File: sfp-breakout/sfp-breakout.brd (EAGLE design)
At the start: 65 x 65 mm, 29 parts, among them IC1 TLV1117-25, J1 694108106102, X1 PINHD-1X4LOCK, X2 PINHD-1X4LOCK

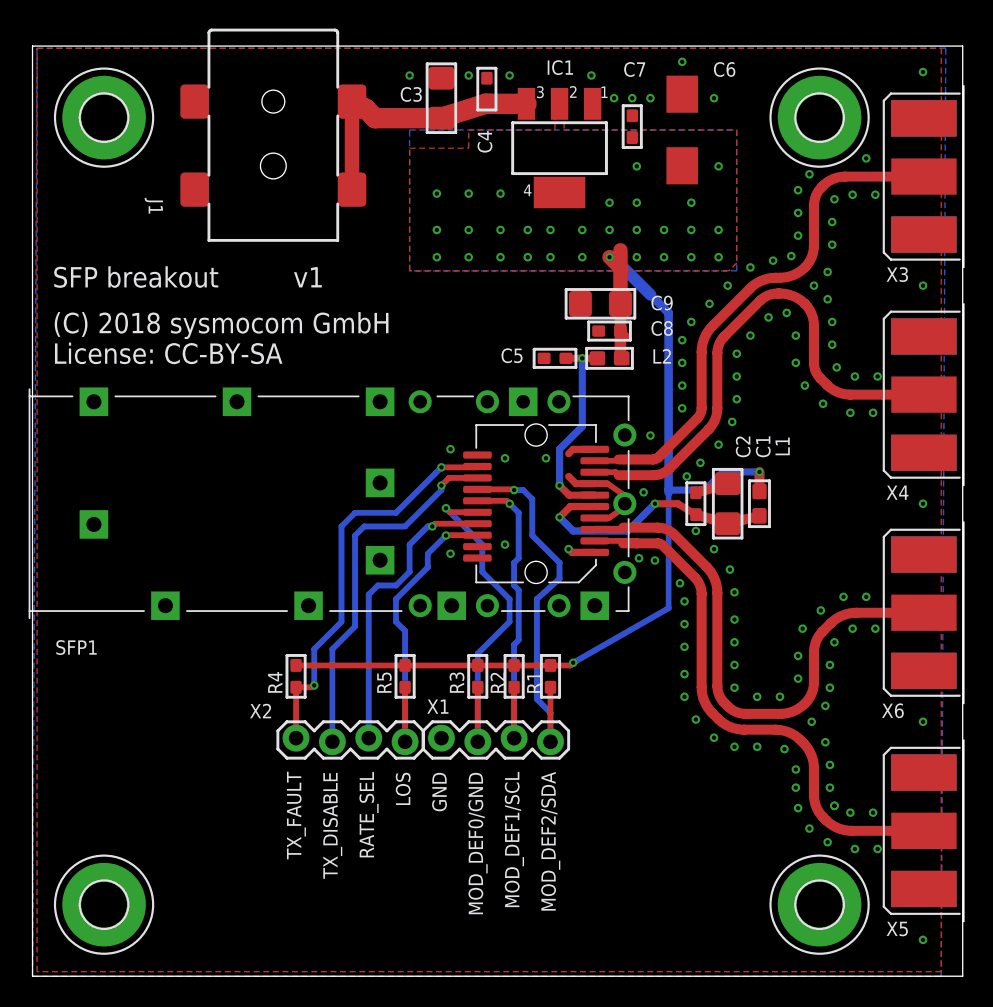
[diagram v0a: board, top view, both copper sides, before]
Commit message: spf: revise both SFP designs (OSM#3313/OSM#3314)
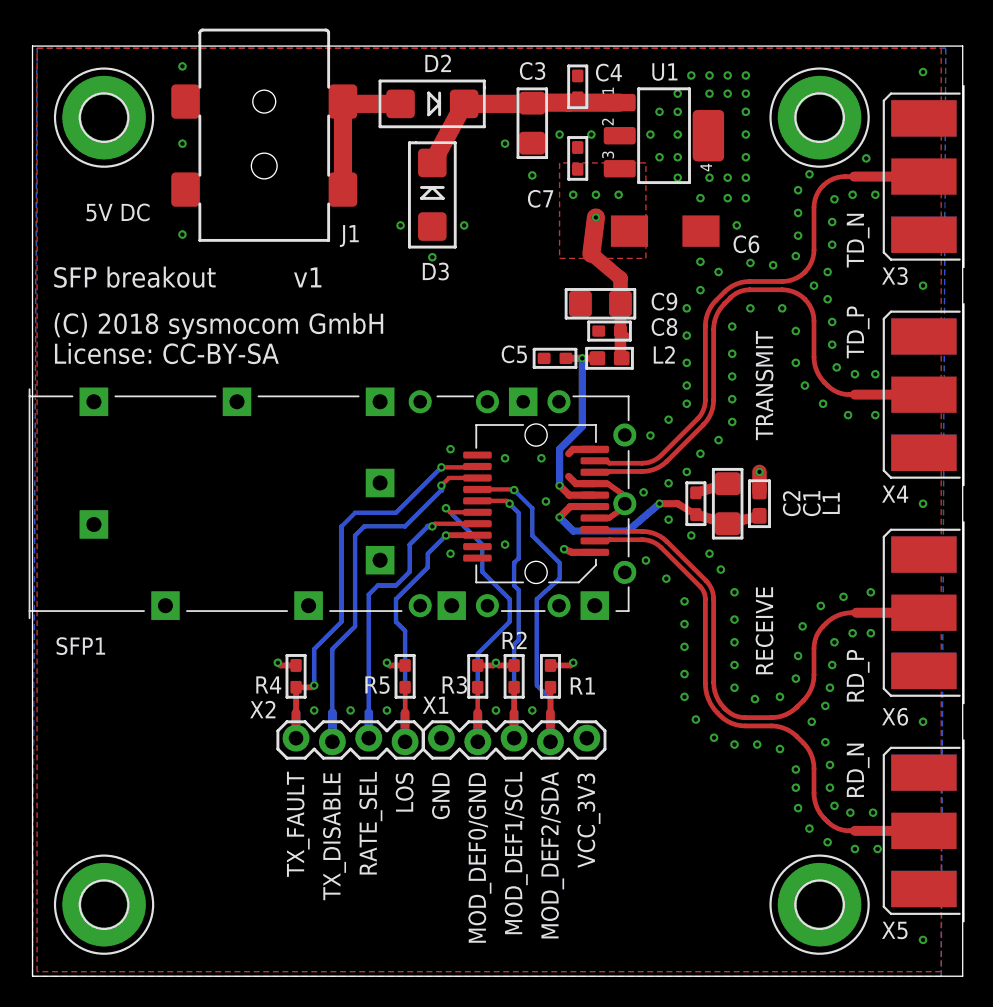
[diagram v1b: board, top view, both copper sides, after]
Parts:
- removed IC1: TLV1117-25, sfp-experimenter:SOT223
- added D2: SS16T3G, sfp-breakout:SMADIODE
- added D3: 824500500, sfp-breakout:SMADIODE
- added U1: LDO-MCP1825S, sfp-breakout:SOT223
- C1, C3, C9: device sfp-experimenter:CPOL1206 -> sfp-breakout:CPOL1206
- C2, C4, C5, C7, C8, R1, R2, R3, R4, R5: device sfp-experimenter:_0603 -> sfp-breakout:_0603
- H1, H2, H3, H4: device sfp-experimenter:3,2-PAD -> sfp-breakout:3,2-PAD
- J1: device sfp-experimenter:694108106102 -> sfp-breakout:694108106102
- L1, L2: device sfp-experimenter:0603 -> sfp-breakout:0603
- SFP1: device sfp-experimenter:SFP_COMBINED -> sfp-breakout:SFP_COMBINED
- X1: value PINHD-1X4LOCK -> PINHD-1X5LOCK; device sfp-experimenter:1X04_LOCK -> sfp-breakout:1X05_LOCK
- X2: device sfp-experimenter:1X04_LOCK -> sfp-breakout:1X04_LOCK
- X3, X4, X5, X6: device sfp-experimenter:SMA-F-S-EDGE -> sfp-breakout:SMA-F-S-EDGE
- moved C6 7.16 mm to (44.2, 52.1), turned to 0 degrees
- moved C3 6.59 mm to (34.9, 59.6), turned to 90 degrees
- moved C4 6.35 mm to (38.1, 62.2)
- moved C7 4.41 mm to (38.1, 57.1)
- moved J1 0.64 mm to (16.2, 66.1)
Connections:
- new net N$1: D2.A, J1.1, J1.1-1
- net +VIN: now also D2.C, D3.C, U1.1; no longer IC1.3, J1.1, J1.1-1
- net GND: now also D3.A, U1.2, U1.4; no longer IC1.1
- net VCC_3V3: now also U1.3; no longer IC1.2, IC1.4
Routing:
- net VCC_3V3: track 71.1 -> 19.9 mm, vias 32 -> 9
- net N$1: track 0.00 -> 10.5 mm
- net +VIN: track 19.6 -> 16.3 mm
- net TX_FAULT: track 28.0 -> 29.8 mm
- net RD_N: track 38.3 -> 37.0 mm
- net TD_N: track 36.0 -> 37.1 mm
- net TD_P: track 35.9 -> 36.8 mm
- net GND: track 14.2 -> 14.5 mm, vias 116 -> 150
- added copper zone on layer 2, net GND
- added copper zone on layer 15, net VCC_3V3
- removed copper zone on layer 16, net VCC_3V3
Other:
- board text added: "5V DC"
- board text added: "RD_N"
- board text added: "RD_P"
- board text added: "RECEIVE"
- board text added: "TD_N"
- board text added: "TD_P"
- board text added: "TRANSMIT"
- board text added: "VCC_3V3"

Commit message: sfp: add LOS, TX_FAULT LEDs + add more supply pinheader on both PCBs
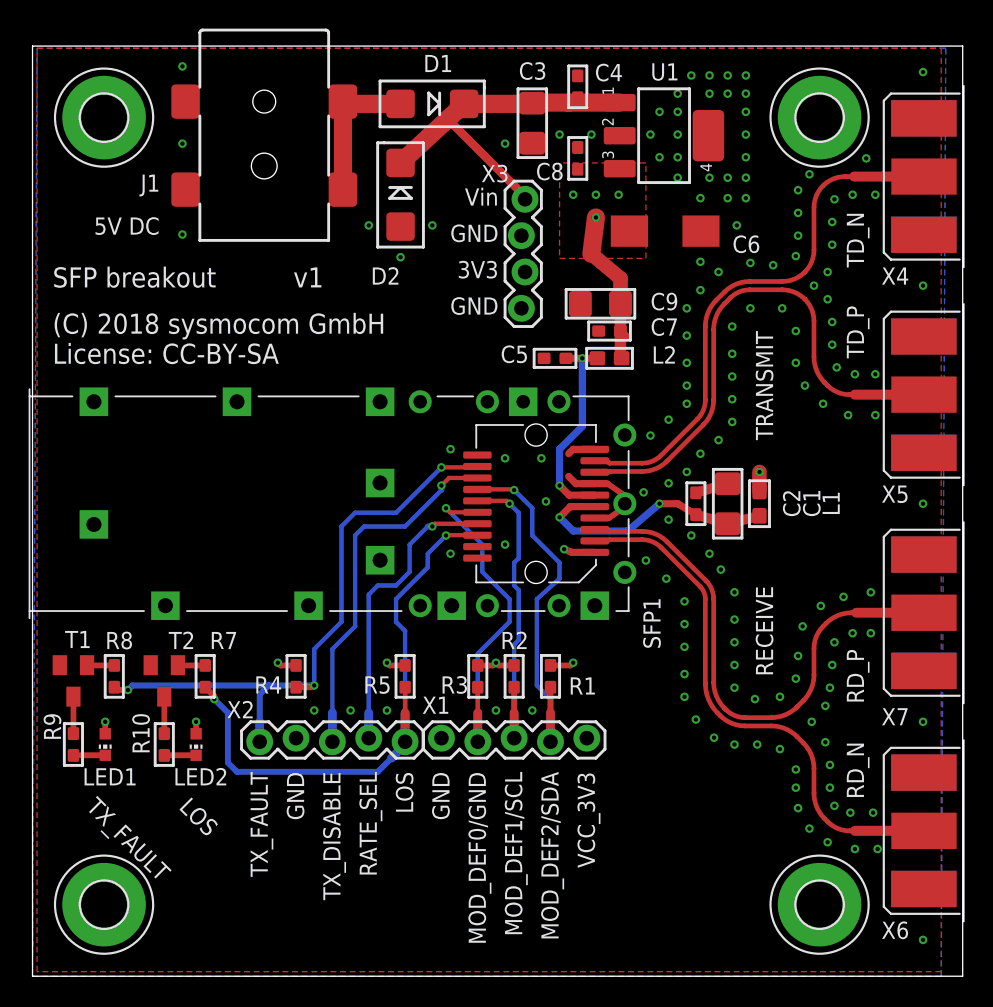
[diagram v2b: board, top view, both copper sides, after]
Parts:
- removed D3: 824500500, sfp-breakout:SMADIODE
- added D1: SS16T3G, sfp-breakout:SMADIODE
- added LED1, LED2: KPH-1608SGC, led:CHIP-LED0603
- added R10, R9: 330, rc-sysmocom:_0603
- added R7, R8: 10k, rc-sysmocom:_0603
- added T1, T2: BC847, transistor:SOT23-BEC
- added X7: (no value), sfp-breakout:SMA-F-S-EDGE
- D2: value SS16T3G -> 824500500
- X2: value PINHD-1X4LOCK -> PINHD-1X5LOCK; device sfp-breakout:1X04_LOCK -> sfp-breakout:1X05_LOCK
- X3: value (none) -> PINHD-1X4LOCK; device sfp-breakout:SMA-F-S-EDGE -> sfp-breakout:1X04_LOCK
- moved X3 30.8 mm to (34.3, 54.3), turned to 270 degrees
- moved X5 30.5 mm to (65.1, 40.6)
- moved X4 15.2 mm to (65.1, 55.9)
- moved X6 15.2 mm to (65.1, 10.2)
- moved C7 12.3 mm to (40.3, 45.1), turned to 180 degrees
- moved C8 12.3 mm to (38.1, 57.1), turned to 90 degrees
- moved D2 6.73 mm to (25.7, 54.6), turned to 270 degrees
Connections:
- new net N$138: R8.1, T1.B
- new net N$139: LED1.C, R9.2
- new net N$141: R9.1, T1.C
- new net N$3: R7.1, T2.B
- new net N$4: LED2.C, R10.2
- new net N$7: R10.1, T2.C
- net +VIN: now also D1.C, X3.1; no longer D3.C
- net GND: now also D2.A, T1.E, T2.E, X2.4, X3.2, X3.4, X7.BG1, X7.BG2, X7.TG1, X7.TG2; no longer D3.A, X3.BG1, X3.BG2, X3.TG1, X3.TG2
- net LOS: now also R7.2
- net N$1: now also D1.A; no longer D2.A
- net RD_N: now also X6.C; no longer X5.C
- net RD_P: now also X7.C; no longer X6.C
- net TD_N: now also X4.C; no longer X3.C
- net TD_P: now also X5.C; no longer X4.C
- net TX_FAULT: now also R8.2, X2.5; no longer X2.4
- net VCC_3V3: now also LED1.A, LED2.A, X3.3
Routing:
- net LOS: track 22.1 -> 41.7 mm, vias 1 -> 2
- net TX_FAULT: track 29.8 -> 42.8 mm, vias 2 -> 3
- net +VIN: track 16.3 -> 25.5 mm
- net N$7: track 0.00 -> 2.58 mm
- net N$141: track 0.00 -> 2.58 mm
- net N$4: track 0.00 -> 2.23 mm
- net N$139: track 0.00 -> 2.23 mm
- net N$138: track 0.00 -> 1.92 mm
- net N$3: track 0.00 -> 1.92 mm
- net VCC_3V3: track 19.9 -> 21.6 mm, vias 9 -> 11
- net GND: vias 150 -> 149
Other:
- board text added: "3V3"
- board text added: "Vin"
